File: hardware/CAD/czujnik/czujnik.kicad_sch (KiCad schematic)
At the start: 9 parts, among them J2 Barrel_Jack, J3 8P8C, U1 Pico

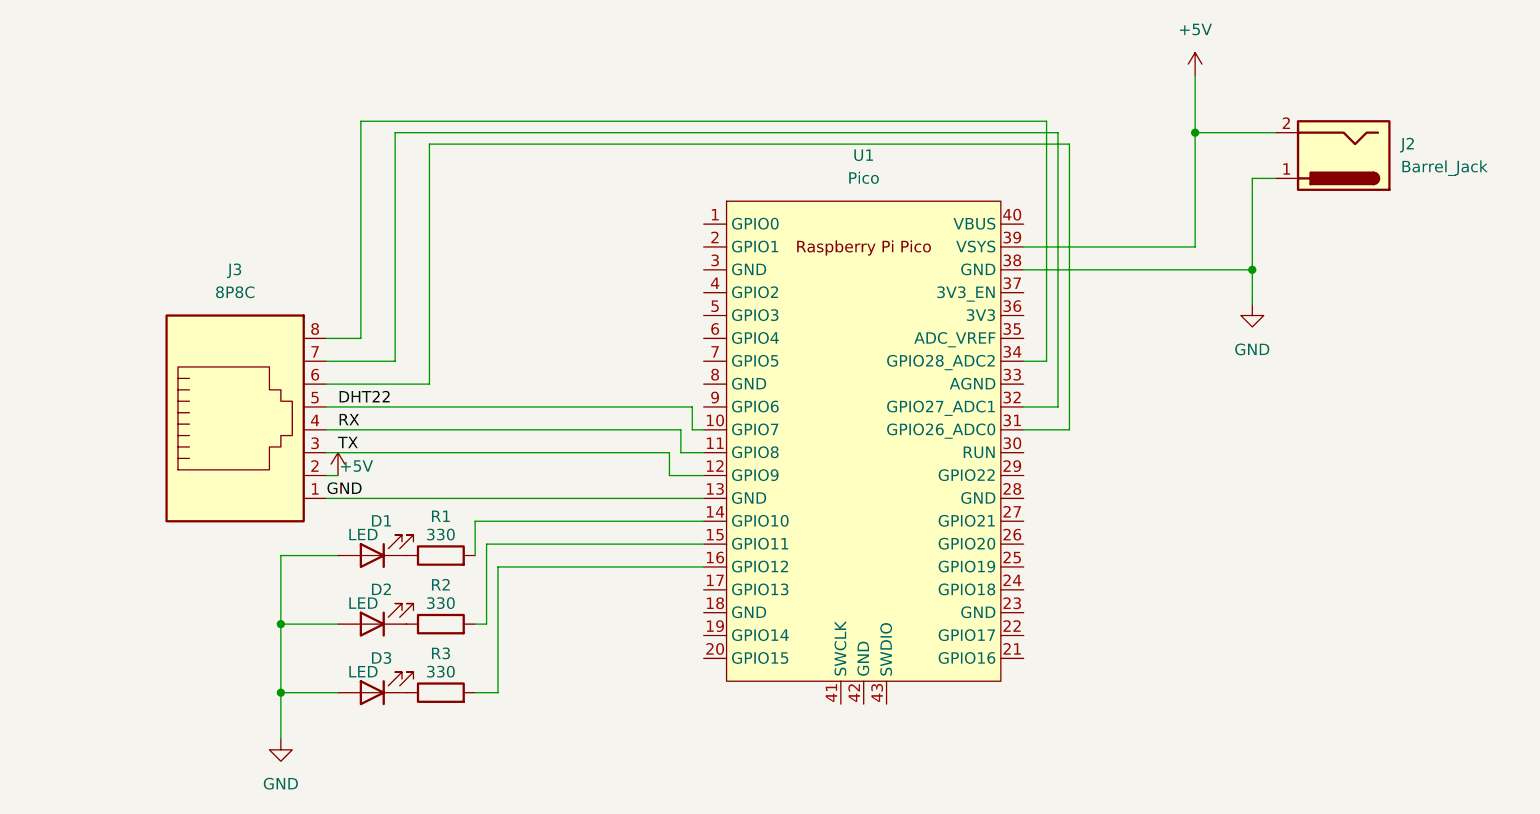
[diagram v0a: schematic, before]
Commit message: refactor PCBs, add gerber files
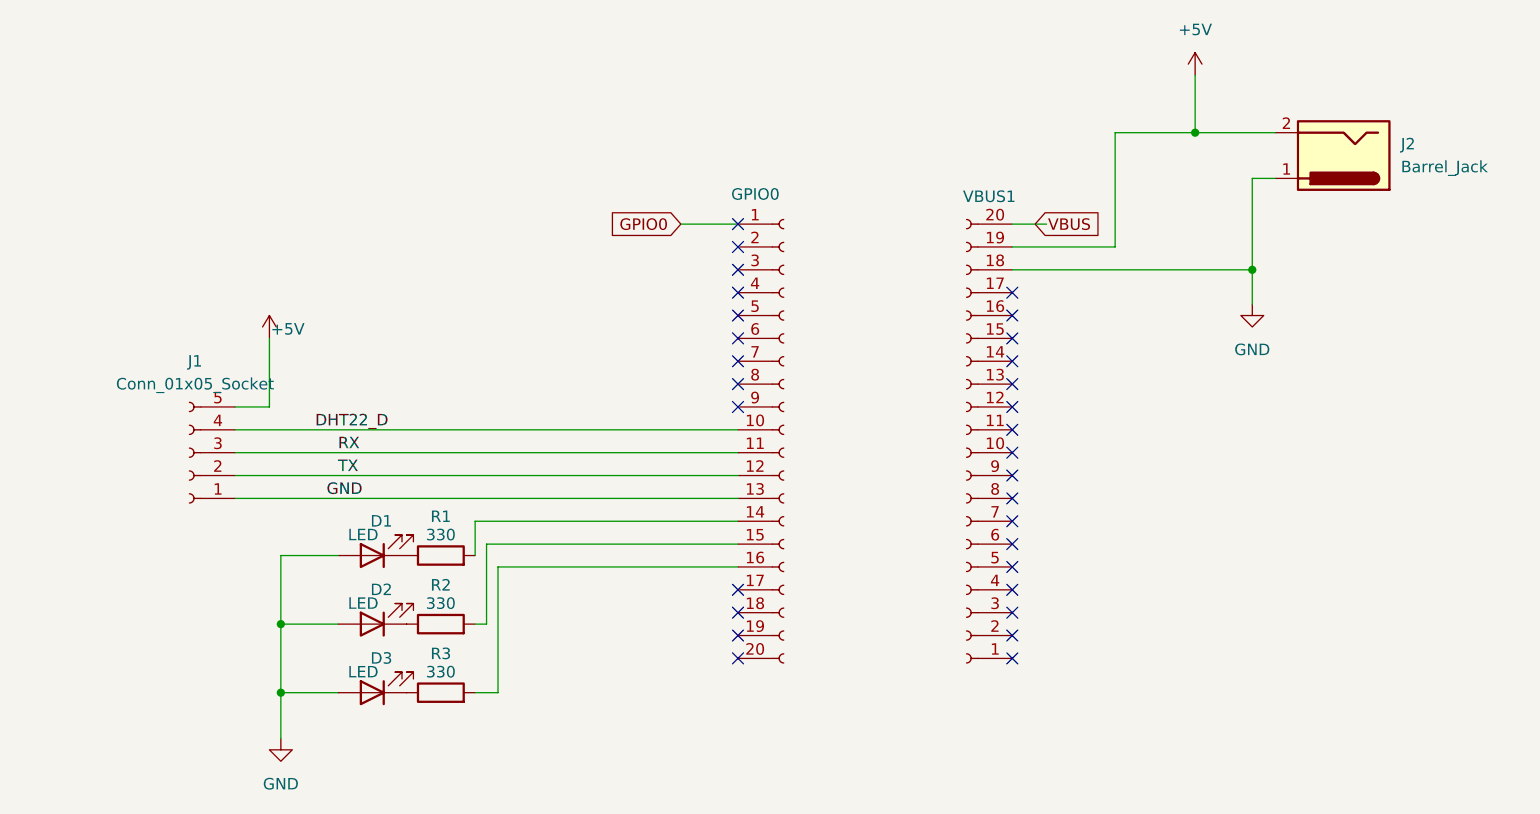
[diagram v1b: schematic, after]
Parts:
- removed J3: 8P8C, Connector_RJ:RJ45_Connfly_DS1128-09-S8xx-S_Horizontal, symbol Connector:8P8C
- removed U1: Pico, MCU_RaspberryPi_and_Boards:RPi_Pico_SMD_TH, symbol MCU_RaspberryPi_and_Boards:Pico
- added GPIO0, VBUS1: Conn_01x20_Socket, Connector_PinSocket_2.54mm:PinSocket_1x20_P2.54mm_Vertical, symbol Connector:Conn_01x20_Socket
- added J1: Conn_01x05_Socket, Connector_PinSocket_2.54mm:PinSocket_1x05_P2.54mm_Vertical, symbol Connector:Conn_01x05_Socket
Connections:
- net +5V: now also J1.5 (Pin_5), VBUS1.19 (Pin_19)
- net GND: now also GPIO0.13 (Pin_13), J1.1 (Pin_1), VBUS1.18 (Pin_18)
- net RX: now also GPIO0.11 (Pin_11), J1.3 (Pin_3)
- net TX: now also GPIO0.12 (Pin_12), J1.2 (Pin_2)
- net at R1.2: now also GPIO0.14 (Pin_14)
- net at R2.2: now also GPIO0.15 (Pin_15)
- net at R3.2: now also GPIO0.16 (Pin_16)
- new net DHT22_D: GPIO0.10 (Pin_10), J1.4 (Pin_4)
- new net GPIO0: GPIO0.1 (Pin_1)
- new net VBUS: VBUS1.20 (Pin_20)
- no-connect marks 0 -> 30

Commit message: add DB9 connectors to PCBs
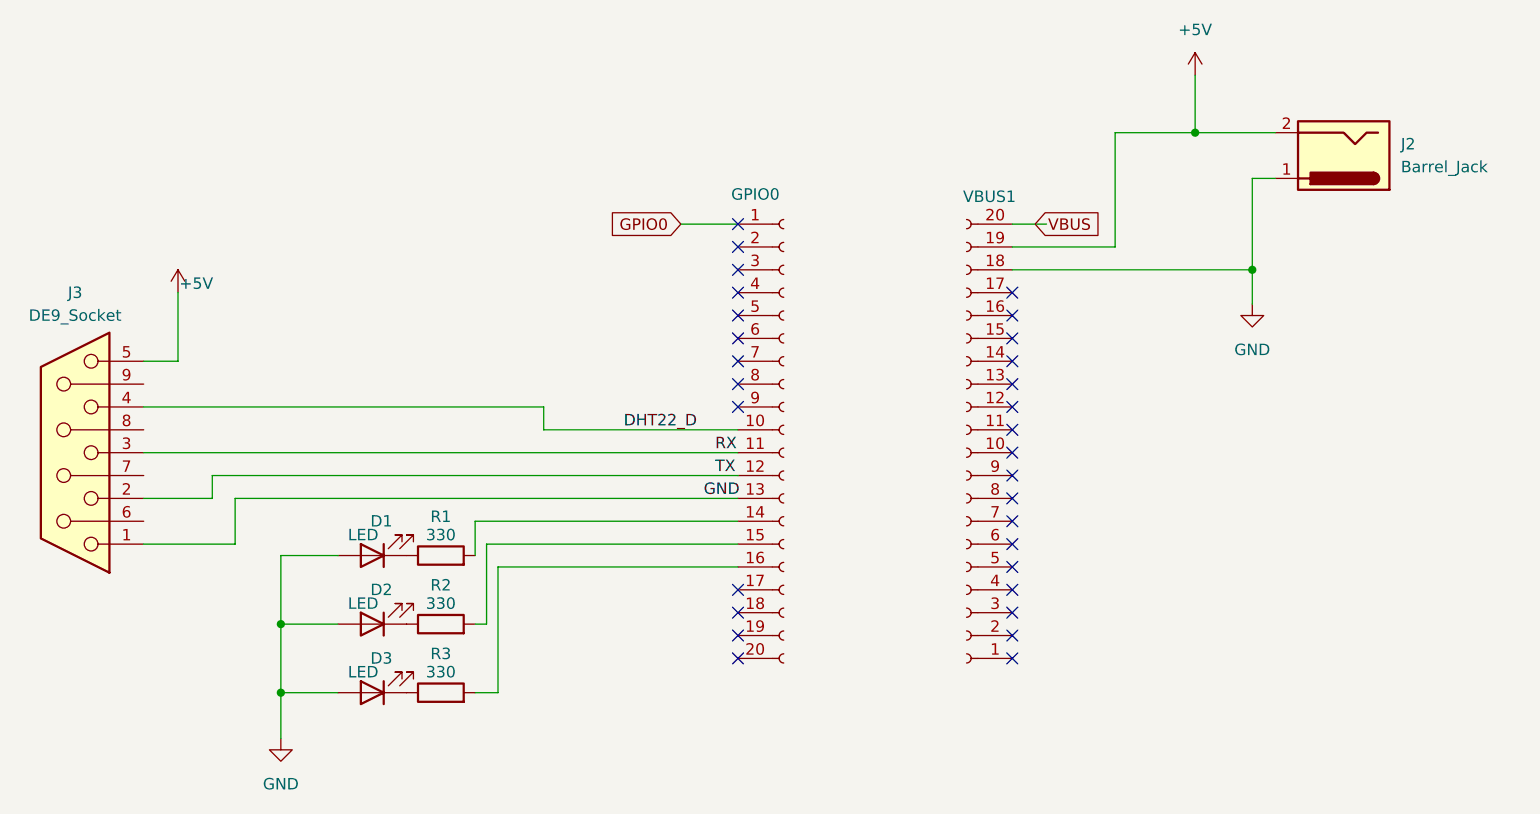
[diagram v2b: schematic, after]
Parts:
- removed J1: Conn_01x05_Socket, Connector_PinSocket_2.54mm:PinSocket_1x05_P2.54mm_Vertical, symbol Connector:Conn_01x05_Socket
- added J3: DE9_Socket, Connector_Dsub:DSUB-9_Socket_Horizontal_P2.77x2.84mm_EdgePinOffset7.70mm_Housed_MountingHolesOffset9.12mm, symbol Connector:DE9_Socket
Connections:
- net +5V: now also J3.5
- net DHT22_D: now also J3.4
- net GND: now also J3.1
- net RX: now also J3.3
- net TX: now also J3.2
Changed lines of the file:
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@@
-	(wire
-		(pts
-			(xy 73.66 82.55) (xy 129.54 82.55)
-		)
-		(stroke
-			(width 0)
-			(type default)
-		)
-	)
 	(wire
 		(pts
@@
 	(wire
 		(pts
-			(xy 77.47 69.85) (xy 77.47 77.47)
+			(xy 67.31 64.77) (xy 67.31 72.39)
 		)
 		(stroke
@@
 	(wire
 		(pts
+			(xy 107.95 77.47) (xy 63.5 77.47)
+		)
+		(stroke
+			(width 0)
+			(type default)
+		)
+	)
+	(wire
+		(pts
 			(xy 78.74 93.98) (xy 85.09 93.98)
 		)
@@
 	(wire
 		(pts
-			(xy 77.47 77.47) (xy 73.66 77.47)
+			(xy 67.31 72.39) (xy 63.5 72.39)
 		)
 		(stroke
@@
 	(wire
 		(pts
+			(xy 63.5 82.55) (xy 129.54 82.55)
+		)
+		(stroke
+			(width 0)
+			(type default)
+		)
+	)
+	(wire
+		(pts
 			(xy 101.6 101.6) (xy 100.33 101.6)
 		)
@@
 	(wire
 		(pts
+			(xy 71.12 85.09) (xy 71.12 87.63)
+		)
+		(stroke
+			(width 0)
+			(type default)
+		)
+	)
+	(wire
+		(pts
+			(xy 73.66 92.71) (xy 63.5 92.71)
+		)
+		(stroke
+			(width 0)
+			(type default)
+		)
+	)
+	(wire
+		(pts
 			(xy 100.33 90.17) (xy 100.33 93.98)
 		)
@@
 	(wire
 		(pts
+			(xy 71.12 85.09) (xy 129.54 85.09)
+		)
+		(stroke
+			(width 0)
+			(type default)
+		)
+	)
+	(wire
+		(pts
 			(xy 186.69 62.23) (xy 186.69 66.04)
 		)
@@
 	(wire
 		(pts
-			(xy 73.66 85.09) (xy 129.54 85.09)
+			(xy 73.66 87.63) (xy 73.66 92.71)
 		)
 		(stroke
@@
 	(wire
 		(pts
+			(xy 107.95 80.01) (xy 107.95 77.47)
+		)
+		(stroke
+			(width 0)
+			(type default)
+		)
+	)
+	(wire
+		(pts
+			(xy 71.12 87.63) (xy 63.5 87.63)
+		)
+		(stroke
+			(width 0)
+			(type default)
+		)
+	)
+	(wire
+		(pts
 			(xy 160.02 62.23) (xy 186.69 62.23)
 		)
@@
 	(wire
 		(pts
-			(xy 73.66 80.01) (xy 129.54 80.01)
+			(xy 107.95 80.01) (xy 129.54 80.01)
 		)
 		(stroke
@@
 	)
 	(label "RX"
-		(at 85.09 82.55 0)
+		(at 127 82.55 0)
 		(effects
 			(font
@@
 	)
 	(label "DHT22_D"
-		(at 82.55 80.01 0)
+		(at 116.84 80.01 0)
 		(effects
 			(font
@@
 	)
 	(label "TX"
-		(at 85.09 85.09 0)
+		(at 127 85.09 0)
 		(effects
 			(font
@@
 	)
 	(label "GND"
-		(at 83.82 87.63 0)
+		(at 125.73 87.63 0)
 		(effects
 			(font
@@
 	(symbol
 		(lib_id "power:+5V")
-		(at 77.47 69.85 0)
+		(at 67.31 64.77 0)
 		(unit 1)
 		(exclude_from_sim no)
@@
 		(dnp no)
 		(property "Reference" "#PWR03"
-			(at 77.47 73.66 0)
+			(at 67.31 68.58 0)
 			(effects
 				(font
@@
 		)
 		(property "Value" "+5V"
-			(at 79.502 68.834 0)
+			(at 69.342 63.754 0)
 			(effects
 				(font
@@
 		)
 		(property "Footprint" ""
-			(at 77.47 69.85 0)
+			(at 67.31 64.77 0)
 			(effects
 				(font
@@
 		)
 		(property "Datasheet" ""
-			(at 77.47 69.85 0)
+			(at 67.31 64.77 0)
 			(effects
 				(font
@@
 		)
 		(property "Description" "Power symbol creates a global label with name \"+5V\""
-			(at 77.47 69.85 0)
+			(at 67.31 64.77 0)
 			(effects
 				(font
@@
 				(path "/65777c98-eabe-4f41-9a87-ebcb45e8604d"
 					(reference "#PWR03")
-					(unit 1)
-				)
-			)
-		)
-	)
-	(symbol
-		(lib_id "Connector:Conn_01x05_Socket")
-		(at 68.58 82.55 180)
-		(unit 1)
-		(exclude_from_sim no)
-		(in_bom yes)
-		(on_board yes)
-		(dnp no)
-		(fields_autoplaced yes)
-		(property "Reference" "J1"
-			(at 69.215 72.39 0)
-			(effects
-				(font
-					(size 1.27 1.27)
-				)
-			)
-		)
-		(property "Value" "Conn_01x05_Socket"
-			(at 69.215 74.93 0)
-			(effects
-				(font
-					(size 1.27 1.27)
-				)
-			)
-		)
-		(property "Footprint" "Connector_PinSocket_2.54mm:PinSocket_1x05_P2.54mm_Vertical"
-			(at 68.58 82.55 0)
-			(effects
-				(font
-					(size 1.27 1.27)
-				)
-				(hide yes)
-			)
-		)
-		(property "Datasheet" "~"
-			(at 68.58 82.55 0)
-			(effects
-				(font
-					(size 1.27 1.27)
-				)
-				(hide yes)
-			)
-		)
-		(property "Description" "Generic connector, single row, 01x05, script generated"
-			(at 68.58 82.55 0)
-			(effects
-				(font
-					(size 1.27 1.27)
-				)
-				(hide yes)
-			)
-		)
-		(pin "5"
-		)
-		(pin "4"
-		)
-		(pin "1"
-		)
-		(pin "2"
-		)
-		(pin "3"
-		)
-		(instances
-			(project ""
-				(path "/65777c98-eabe-4f41-9a87-ebcb45e8604d"
-					(reference "J1")
 					(unit 1)
 				)
@@
 					(unit 1)
 				)
+			)
+		)
+	)
+	(symbol
+		(lib_id "Connector:DE9_Socket")
+		(at 55.88 82.55 180)
+		(unit 1)
+		(exclude_from_sim no)
+		(in_bom yes)
+		(on_board yes)
+		(dnp no)
+		(fields_autoplaced yes)
+		(property "Reference" "J3"
+			(at 55.88 64.77 0)
+			(effects
+				(font
+					(size 1.27 1.27)
+				)
+			)
+		)
+		(property "Value" "DE9_Socket"
+			(at 55.88 67.31 0)
+			(effects
+				(font
+					(size 1.27 1.27)
+				)
+			)
+		)
+		(property "Footprint" "Connector_Dsub:DSUB-9_Socket_Horizontal_P2.77x2.84mm_EdgePinOffset7.70mm_Housed_MountingHolesOffset9.12mm"
+			(at 55.88 82.55 0)
+			(effects
+				(font
+					(size 1.27 1.27)
+				)
+				(hide yes)
+			)
+		)
+		(property "Datasheet" "~"
+			(at 55.88 82.55 0)
+			(effects
+				(font
+					(size 1.27 1.27)
+				)
+				(hide yes)
+			)
+		)
+		(property "Description" "9-pin D-SUB connector, socket (female)"
+			(at 55.88 82.55 0)
+			(effects
+				(font
+					(size 1.27 1.27)
+				)
+				(hide yes)
+			)
+		)
+		(pin "2"
+		)
+		(pin "4"
+		)
+		(pin "1"
+		)
+		(pin "7"
+		)
+		(pin "3"
+		)
+		(pin "6"
+		)
+		(pin "8"
+		)
+		(pin "9"
+		)
+		(pin "5"
+		)
+		(instances
+			(project ""
+				(path "/65777c98-eabe-4f41-9a87-ebcb45e8604d"
+					(reference "J3")
+					(unit 1)
+				)
